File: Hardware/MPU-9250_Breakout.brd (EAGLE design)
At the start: 17 x 17.8 mm, 18 parts, among them U1 MPU-9250

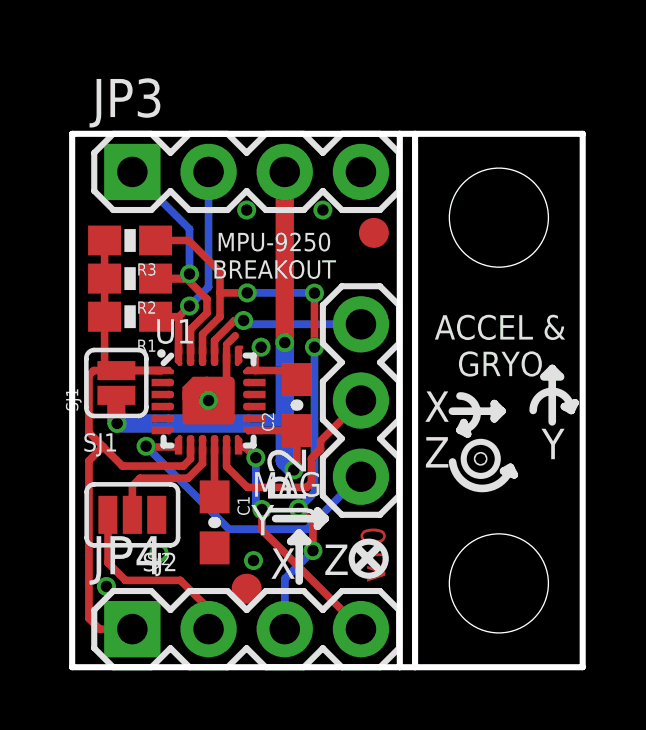
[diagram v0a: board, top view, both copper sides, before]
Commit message: Removed bits of dimension on v-score
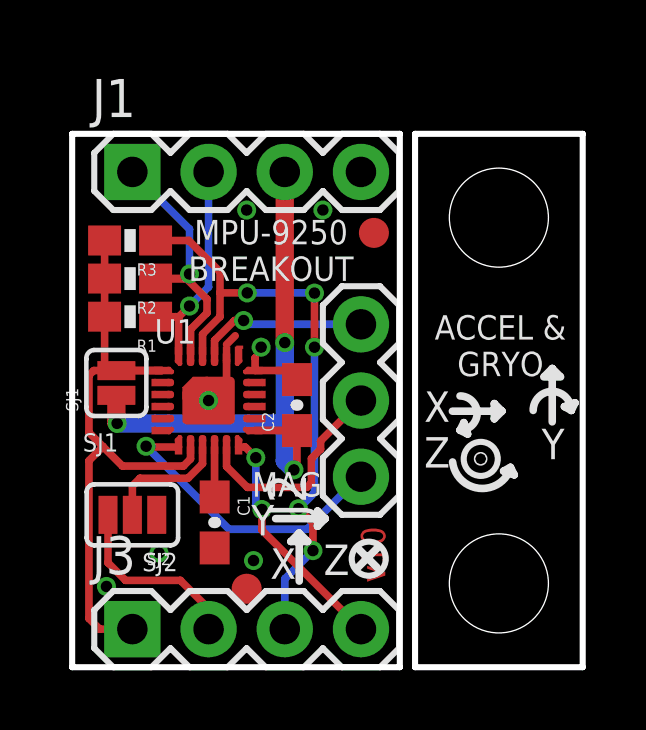
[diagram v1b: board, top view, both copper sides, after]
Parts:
- renumbered JP2 to J2, JP3 to J1, JP4 to J3
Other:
- board text added: "Don't cut v-score in production!"
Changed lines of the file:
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@@
 <layer number="29" name="tStop" color="7" fill="3" visible="no" active="yes"/>
 <layer number="30" name="bStop" color="7" fill="6" visible="no" active="yes"/>
-<layer number="31" name="tCream" color="7" fill="4" visible="no" active="yes"/>
+<layer number="31" name="tCream" color="7" fill="4" visible="yes" active="yes"/>
 <layer number="32" name="bCream" color="7" fill="5" visible="no" active="yes"/>
 <layer number="33" name="tFinish" color="6" fill="3" visible="no" active="yes"/>
@@
 <layer number="37" name="tTest" color="7" fill="1" visible="no" active="yes"/>
 <layer number="38" name="bTest" color="7" fill="1" visible="no" active="yes"/>
-<layer number="39" name="tKeepout" color="4" fill="11" visible="no" active="yes"/>
-<layer number="40" name="bKeepout" color="1" fill="11" visible="no" active="yes"/>
+<layer number="39" name="tKeepout" color="4" fill="11" visible="yes" active="yes"/>
+<layer number="40" name="bKeepout" color="1" fill="11" visible="yes" active="yes"/>
 <layer number="41" name="tRestrict" color="4" fill="10" visible="no" active="yes"/>
 <layer number="42" name="bRestrict" color="1" fill="10" visible="no" active="yes"/>
@@
 <layer number="45" name="Holes" color="7" fill="1" visible="yes" active="yes"/>
 <layer number="46" name="Milling" color="3" fill="1" visible="no" active="yes"/>
-<layer number="47" name="Measures" color="7" fill="1" visible="no" active="yes"/>
+<layer number="47" name="Measures" color="7" fill="1" visible="yes" active="yes"/>
 <layer number="48" name="Document" color="7" fill="1" visible="no" active="yes"/>
 <layer number="49" name="Reference" color="7" fill="1" visible="yes" active="yes"/>
@@
 <board>
 <plain>
-<text x="8.4328" y="-13.5382" size="1.778" layer="51">&gt;DESIGNER</text>
+<text x="8.4328" y="-13.5382" size="1.778" layer="51" font="vector">&gt;DESIGNER</text>
 <text x="10.4394" y="2.8194" size="0.8128" layer="1" font="vector" ratio="18" rot="R90">&gt;VERSION</text>
 <wire x1="0" y1="0" x2="10.922" y2="0" width="0.2032" layer="20"/>
@@
 <dimension x1="0" y1="17.78" x2="10.922" y2="17.78" x3="5.461" y3="18.9484" textsize="1.778" textratio="15" layer="47" unit="inch"/>
 <dimension x1="14.224" y1="14.986" x2="0" y2="0" x3="7.112" y3="-3.048" textsize="1.778" textratio="15" layer="47" dtype="horizontal" unit="inch"/>
-<wire x1="10.922" y1="17.78" x2="11.43" y2="17.78" width="0.2032" layer="20"/>
-<wire x1="10.922" y1="0" x2="11.43" y2="0" width="0.2032" layer="20"/>
 <text x="9.6266" y="15.113" size="0.8128" layer="22" font="vector" ratio="15" rot="SMR270" align="center-left">GND</text>
 <text x="8.2296" y="11.43" size="0.8128" layer="22" font="vector" ratio="15" rot="SMR0" align="center-left">AUXDA</text>
@@
 <wire x1="9.525" y1="3.3274" x2="10.16" y2="3.9624" width="0.254" layer="21"/>
 <text x="2.54" y="12.4714" size="0.8128" layer="22" font="vector" ratio="15" rot="SMR0" align="center-left">A&amp;G</text>
-<text x="6.731" y="13.716" size="0.6096" layer="21" font="vector" ratio="15" align="center">MPU-9250
+<text x="6.6294" y="13.8938" size="0.8128" layer="21" font="vector" ratio="15" align="center">MPU-9250
 BREAKOUT</text>
 <rectangle x1="6.32" y1="8.165" x2="6.45" y2="8.415" layer="1"/>
@@
 <rectangle x1="2.645" y1="7.765" x2="2.775" y2="8.015" layer="1"/>
 <rectangle x1="5.47" y1="10.61" x2="5.7" y2="10.72" layer="1"/>
+<text x="11.3284" y="19.3548" size="1.016" layer="51" font="vector" ratio="15">Don't cut v-score in production!</text>
 </plain>
 <attributes>
@@
 <element name="FID1" library="SparkFun-Aesthetics" package="FIDUCIAL-1X2" value="FIDUCIAL1X2" x="10.0584" y="14.478"/>
 <element name="FID2" library="SparkFun-Aesthetics" package="FIDUCIAL-1X2" value="FIDUCIAL1X2" x="5.8166" y="2.6162"/>
-<element name="JP2" library="SparkFun-Connectors" package="1X03" value="" x="9.6266" y="6.35" rot="R90"/>
-<element name="JP3" library="SparkFun-Connectors" package="1X04" value="" x="2.0066" y="16.51"/>
-<element name="JP4" library="SparkFun-Connectors" package="1X04" value="" x="2.0066" y="1.27"/>
+<element name="J2" library="SparkFun-Connectors" package="1X03" value="" x="9.6266" y="6.35" rot="R90"/>
+<element name="J1" library="SparkFun-Connectors" package="1X04" value="" x="2.0066" y="16.51">
+<attribute name="PROD_ID" value="CONN-09696" x="2.0066" y="16.51" size="1.778" layer="27" display="off"/>
+</element>
+<element name="J3" library="SparkFun-Connectors" package="1X04" value="" x="2.0066" y="1.27">
+<attribute name="PROD_ID" value="CONN-09696" x="2.0066" y="1.27" size="1.778" layer="27" display="off"/>
+</element>
 </elements>
 <signals>
@@
 <contactref element="C2" pad="2"/>
 <contactref element="SJ2" pad="1"/>
-<contactref element="JP3" pad="4"/>
+<contactref element="J1" pad="4"/>
 <wire x1="6.0966" y1="9.89" x2="6.0966" y2="10.3118" width="0.254" layer="1"/>
 <wire x1="6.0966" y1="10.3118" x2="6.096" y2="10.3124" width="0.254" layer="1"/>
@@
 <contactref element="SJ1" pad="1"/>
 <contactref element="C2" pad="1"/>
-<contactref element="JP3" pad="3"/>
+<contactref element="J1" pad="3"/>
 <wire x1="6.0966" y1="7.89" x2="7.4906" y2="7.89" width="0.254" layer="1"/>
 <wire x1="7.4906" y1="7.89" x2="7.493" y2="7.8876" width="0.254" layer="1"/>
@@
 <wire x1="3.7084" y1="6.7056" x2="3.9466" y2="6.9438" width="0.254" layer="1"/>
 <wire x1="3.9466" y1="6.9438" x2="3.9466" y2="7.34" width="0.254" layer="1"/>
-<contactref element="JP4" pad="1"/>
+<contactref element="J3" pad="1"/>
 <wire x1="2.0066" y1="1.27" x2="0.9144" y2="1.27" width="0.254" layer="1"/>
 <wire x1="0.9144" y1="1.27" x2="0.5588" y2="1.6256" width="0.254" layer="1"/>
@@
 <signal name="INT">
 <contactref element="U1" pad="12"/>
-<contactref element="JP4" pad="4"/>
+<contactref element="J3" pad="4"/>
 <wire x1="5.5466" y1="7.34" x2="5.7664" y2="7.34" width="0.254" layer="1"/>
 <wire x1="5.7664" y1="7.34" x2="6.1214" y2="6.985" width="0.254" layer="1"/>
@@
 <signal name="FSYNC">
 <contactref element="U1" pad="11"/>
-<contactref element="JP2" pad="2"/>
+<contactref element="J2" pad="2"/>
 <wire x1="5.1466" y1="7.34" x2="5.1466" y2="6.6898" width="0.254" layer="1"/>
 <wire x1="5.1466" y1="6.6898" x2="5.842" y2="5.9944" width="0.254" layer="1"/>
@@
 <signal name="AUX_CL">
 <contactref element="U1" pad="7"/>
-<contactref element="JP2" pad="1"/>
+<contactref element="J2" pad="1"/>
 <wire x1="3.5466" y1="7.34" x2="2.4898" y2="7.34" width="0.254" layer="1"/>
 <via x="2.4638" y="7.366" extent="1-16" drill="0.381"/>
@@
 <signal name="AUX_DA">
 <contactref element="U1" pad="21"/>
-<contactref element="JP2" pad="3"/>
+<contactref element="J2" pad="3"/>
 <via x="5.715" y="11.557" extent="1-16" drill="0.381"/>
 <wire x1="5.715" y1="11.557" x2="5.842" y2="11.43" width="0.254" layer="16"/>
@@
 <contactref element="R3" pad="1"/>
 <wire x1="3.8862" y1="14.224" x2="2.7804" y2="14.224" width="0.254" layer="1"/>
-<contactref element="JP4" pad="3"/>
+<contactref element="J3" pad="3"/>
 <wire x1="4.3466" y1="10.44" x2="4.3466" y2="11.103" width="0.254" layer="1"/>
 <wire x1="4.3466" y1="11.103" x2="4.9276" y2="11.684" width="0.254" layer="1"/>
@@
 <contactref element="R2" pad="1"/>
 <wire x1="3.81" y1="12.954" x2="2.7804" y2="12.954" width="0.254" layer="1"/>
-<contactref element="JP3" pad="1"/>
+<contactref element="J1" pad="1"/>
 <wire x1="3.9466" y1="10.44" x2="3.9466" y2="11.2618" width="0.254" layer="1"/>
 <wire x1="4.4958" y1="11.811" x2="4.4958" y2="12.2682" width="0.254" layer="1"/>
@@
 <contactref element="U1" pad="24"/>
 <contactref element="R1" pad="1"/>
-<contactref element="JP3" pad="2"/>
+<contactref element="J1" pad="2"/>
 <wire x1="3.5466" y1="10.44" x2="3.5466" y2="11.5918" width="0.254" layer="1"/>
 <wire x1="3.5466" y1="11.5918" x2="3.4544" y2="11.684" width="0.254" layer="1"/>
@@
 <signal name="AD0/SDO">
 <contactref element="SJ2" pad="3"/>
-<contactref element="JP4" pad="2"/>
+<contactref element="J3" pad="2"/>
 <wire x1="1.1938" y1="5.08" x2="1.1938" y2="3.4798" width="0.254" layer="1"/>
 <wire x1="1.1938" y1="3.4798" x2="1.778" y2="2.8956" width="0.254" layer="1"/>
